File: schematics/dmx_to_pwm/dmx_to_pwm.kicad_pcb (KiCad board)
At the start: 2 copper layers, 11 parts, among them J4 PJ-031D, SW1 SW_SPST, SW2 SW_SPDT, U1 SN75176AP, U2 6N137, U3 6N137, U4 SN75176AP, U5 LM7812_TO220

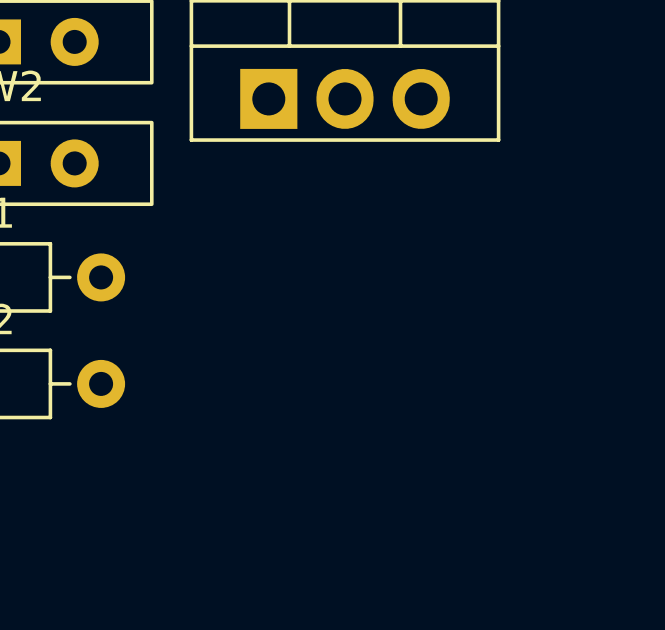
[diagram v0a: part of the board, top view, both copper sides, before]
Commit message: #5 improved schematics
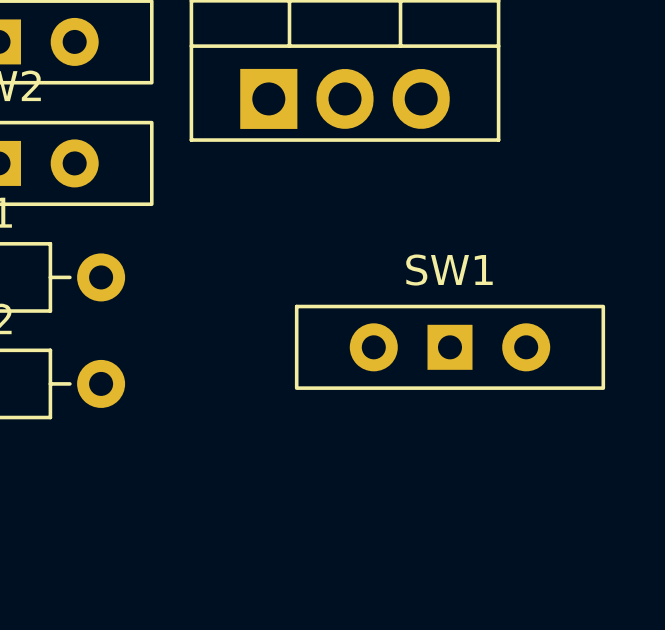
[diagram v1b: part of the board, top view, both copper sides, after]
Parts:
- added SW1: SW_SPDT, Button_Switch_THT:SW_Slide-03_Wuerth-WS-SLTV_10x2.5x6.4_P2.54mm, F.Cu at (109.2, 43.2)
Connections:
- D1 pad 2: Net-(D1-A) -> unconnected-(D1-A-Pad2)
- J4 pad 3: Net-(SW1-B) -> Net-(C3-Pad1)
- U5 pad 1: Net-(SW1-A) -> Net-(U5-VI)
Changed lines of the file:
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@@
 	(net 49 "Net-(U4-A)")
 	(net 50 "unconnected-(J4-Pad2)")
+	(net 51 "unconnected-(D1-A-Pad2)")
+	(net 52 "Net-(C3-Pad1)")
+	(net 53 "unconnected-(SW1-C-Pad2)")
+	(net 54 "Net-(U5-VI)")
 	(footprint "Button_Switch_THT:SW_Slide-03_Wuerth-WS-SLTV_10x2.5x6.4_P2.54mm"
 		(layer "F.Cu")
@@
 			(layers "*.Cu" "*.Mask")
 			(remove_unused_layers no)
-			(net 33 "Net-(SW1-B)")
+			(net 52 "Net-(C3-Pad1)")
 			(pinfunction "3")
 			(pintype "passive")
@@
 			(offset
 				(xyz -5.329999844 -0.09999999999 -2.579999885)
+			)
+			(scale
+				(xyz 1 1 1)
+			)
+			(rotate
+				(xyz 0 0 0)
+			)
+		)
+	)
+	(footprint "Button_Switch_THT:SW_Slide-03_Wuerth-WS-SLTV_10x2.5x6.4_P2.54mm"
+		(layer "F.Cu")
+		(at 109.22 43.18)
+		(descr "Wuerth, WS-SLTV, 450301014042, https://www.we-online.com/components/products/datasheet/450301014042.pdf")
+		(tags "switch single-pole double-throw SPDT würth wurth")
+		(property "Reference" "SW1"
+			(at 0 -2.54 0)
+			(layer "F.SilkS")
+			(effects
+				(font
+					(size 1 1)
+					(thickness 0.15)
+				)
+			)
+		)
+		(property "Value" "SW_SPDT"
+			(at 0 3.81 0)
+			(layer "F.Fab")
+			(effects
+				(font
+					(size 1 1)
+					(thickness 0.15)
+				)
+			)
+		)
+		(property "Footprint" "Button_Switch_THT:SW_Slide-03_Wuerth-WS-SLTV_10x2.5x6.4_P2.54mm"
+			(at 0 0 0)
+			(unlocked yes)
+			(layer "F.Fab")
+			(hide yes)
+			(effects
+				(font
+					(size 1.27 1.27)
+				)
+			)
+		)
+		(property "Datasheet" "https://www.we-online.com/components/products/datasheet/450301014042.pdf"
+			(at 0 0 0)
+			(unlocked yes)
+			(layer "F.Fab")
+			(hide yes)
+			(effects
+				(font
+					(size 1.27 1.27)
+				)
+			)
+		)
+		(property "Description" "Switch slide, single pole double throw"
+			(at 0 0 0)
+			(unlocked yes)
+			(layer "F.Fab")
+			(hide yes)
+			(effects
+				(font
+					(size 1.27 1.27)
+				)
+			)
+		)
+		(property ki_fp_filters "SW*Wuerth*WS*SLTV*10x2.5x6.4*P2.54mm*")
+		(sheetname "Root")
+		(sheetfile "dmx_to_pwm.kicad_sch")
+		(attr through_hole)
+		(fp_rect
+			(start -5.11 -1.36)
+			(end 5.11 1.36)
+			(stroke
+				(width 0.12)
+				(type default)
+			)
+			(fill none)
+			(layer "F.SilkS")
+		)
+		(fp_rect
+			(start -5.25 -1.5)
+			(end 5.25 1.5)
+			(stroke
+				(width 0.05)
+				(type default)
+			)
+			(fill none)
+			(layer "F.CrtYd")
+		)
+		(fp_rect
+			(start -5 -1.25)
+			(end 5 1.25)
+			(stroke
+				(width 0.1)
+				(type default)
+			)
+			(fill none)
+			(layer "F.Fab")
+		)
+		(fp_text user "${REFERENCE}"
+			(at 0 2.54 0)
+			(layer "F.Fab")
+			(effects
+				(font
+					(size 1 1)
+					(thickness 0.15)
+				)
+			)
+		)
+		(pad "1" thru_hole rect
+			(at 0 0)
+			(size 1.5 1.5)
+			(drill 0.8)
+			(layers "*.Cu" "*.Mask")
+			(remove_unused_layers no)
+			(net 33 "Net-(SW1-B)")
+			(pinfunction "B")
+			(pintype "passive")
+		)
+		(pad "2" thru_hole circle
+			(at -2.54 0)
+			(size 1.6 1.6)
+			(drill 0.8)
+			(layers "*.Cu" "*.Mask")
+			(remove_unused_layers no)
+			(net 53 "unconnected-(SW1-C-Pad2)")
+			(pinfunction "C")
+			(pintype "passive")
+		)
+		(pad "3" thru_hole circle
+			(at 2.54 0)
+			(size 1.6 1.6)
+			(drill 0.8)
+			(layers "*.Cu" "*.Mask")
+			(remove_unused_layers no)
+			(net 20 "VIN")
+			(pinfunction "A")
+			(pintype "passive")
+		)
+		(model "${KICAD8_3DMODEL_DIR}/Button_Switch_THT.3dshapes/SW_Slide-03_Wuerth-WS-SLTV_10x2.5x6.4_P2.54mm.wrl"
+			(offset
+				(xyz 0 0 0)
 			)
 			(scale
@@
 			(layers "*.Cu" "*.Mask")
 			(remove_unused_layers no)
-			(net 32 "Net-(SW1-A)")
+			(net 54 "Net-(U5-VI)")
 			(pinfunction "VI")
 			(pintype "power_in")
@@
 			(layers "*.Cu" "*.Mask")
 			(remove_unused_layers no)
-			(net 30 "Net-(D1-A)")
+			(net 51 "unconnected-(D1-A-Pad2)")
 			(pinfunction "A")
 			(pintype "passive")

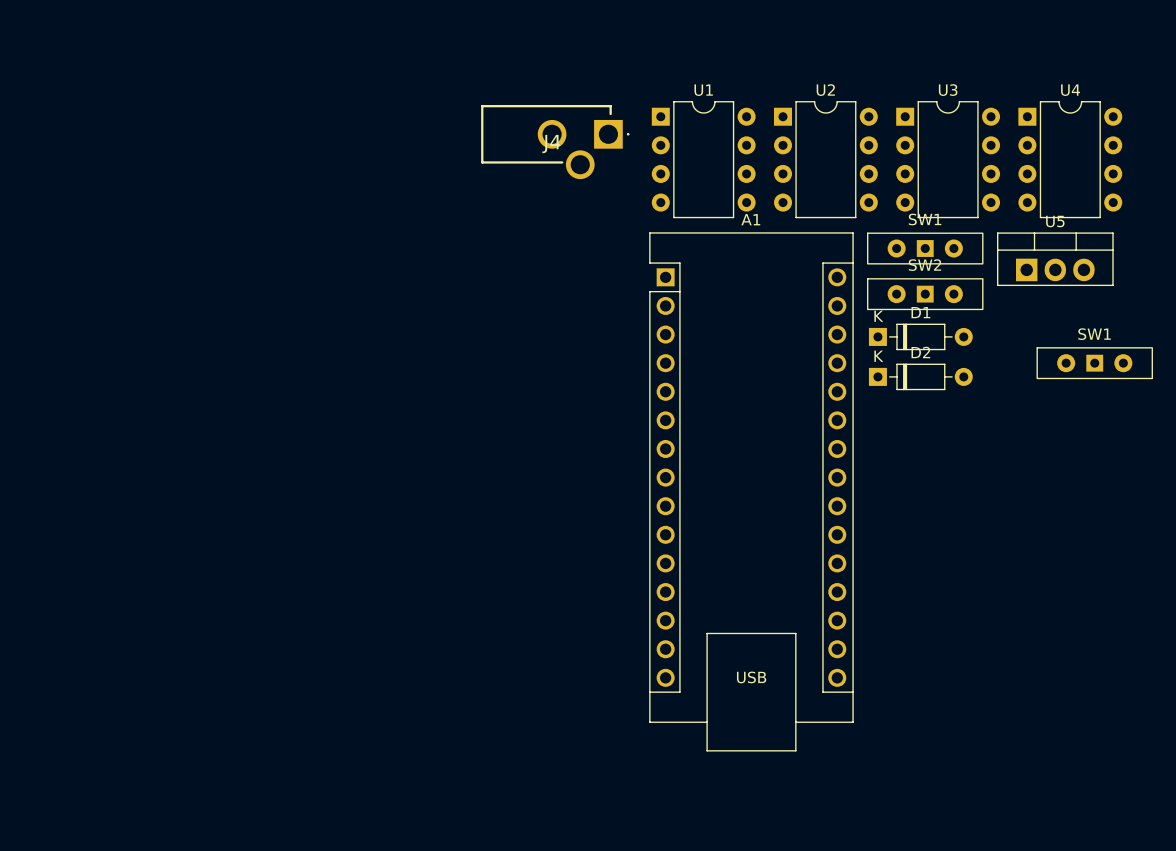
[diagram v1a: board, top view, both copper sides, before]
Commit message: updated schematics, added laser module blender file
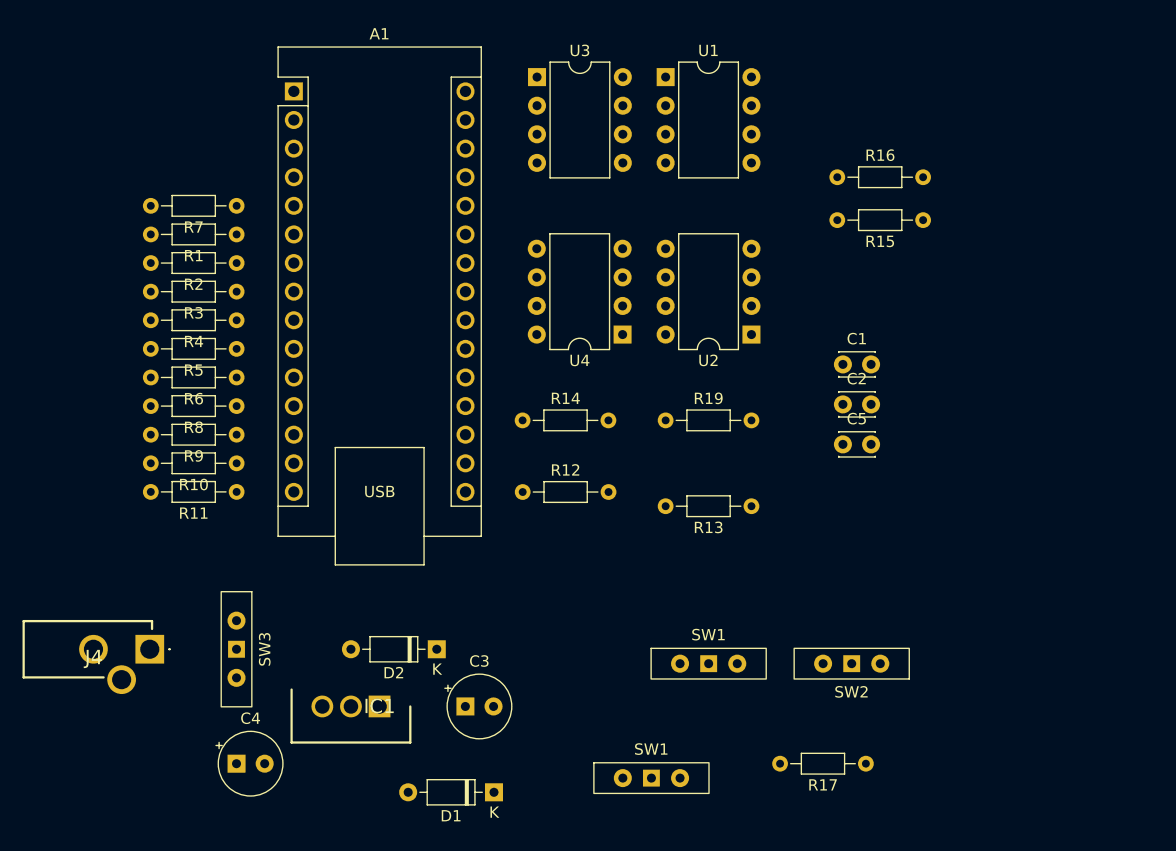
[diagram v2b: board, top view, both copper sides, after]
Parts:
- removed U5: LM7812_TO220, Package_TO_SOT_THT:TO-220-3_Vertical
- added C1: 100nF, Capacitor_THT:C_Disc_D3.0mm_W2.0mm_P2.50mm, F.Cu at (86.9, 43.3)
- added C2: 100nF, Capacitor_THT:C_Disc_D3.0mm_W2.0mm_P2.50mm, F.Cu at (86.9, 46.8)
- added C3: 10uF, Capacitor_THT:CP_Radial_Tantal_D5.5mm_P2.50mm, F.Cu at (53.3, 73.7)
- added C4: 330nF, Capacitor_THT:CP_Radial_Tantal_D5.5mm_P2.50mm, F.Cu at (33.0, 78.7)
- added C5: 100nF, Capacitor_THT:C_Disc_D3.0mm_W2.0mm_P2.50mm, F.Cu at (86.9, 50.4)
- added IC1: LM1085IT-12_NOPB, Lasers:TO254P470X1028X1955-3P, F.Cu at (45.7, 73.7)
- added R1: 1K, Resistor_THT:R_Axial_DIN0204_L3.6mm_D1.6mm_P7.62mm_Horizontal, F.Cu at (33.0, 31.8)
- added R10: 1K, Resistor_THT:R_Axial_DIN0204_L3.6mm_D1.6mm_P7.62mm_Horizontal, F.Cu at (33.0, 52.1)
- added R11: 1K, Resistor_THT:R_Axial_DIN0204_L3.6mm_D1.6mm_P7.62mm_Horizontal, F.Cu at (33.0, 54.6)
- added R12: 1K, Resistor_THT:R_Axial_DIN0204_L3.6mm_D1.6mm_P7.62mm_Horizontal, F.Cu at (58.4, 54.6)
- added R13: 470, Resistor_THT:R_Axial_DIN0204_L3.6mm_D1.6mm_P7.62mm_Horizontal, F.Cu at (78.7, 55.9)
- added R14: 4.7K, Resistor_THT:R_Axial_DIN0204_L3.6mm_D1.6mm_P7.62mm_Horizontal, F.Cu at (58.4, 48.3)
- added R15: 133, Resistor_THT:R_Axial_DIN0204_L3.6mm_D1.6mm_P7.62mm_Horizontal, F.Cu at (94.0, 30.5)
- added R16: 562, Resistor_THT:R_Axial_DIN0204_L3.6mm_D1.6mm_P7.62mm_Horizontal, F.Cu at (86.4, 26.7)
- added R17: 562, Resistor_THT:R_Axial_DIN0204_L3.6mm_D1.6mm_P7.62mm_Horizontal, F.Cu at (88.9, 78.7)
- added R19: 4.7K, Resistor_THT:R_Axial_DIN0204_L3.6mm_D1.6mm_P7.62mm_Horizontal, F.Cu at (71.1, 48.3)
- added R2: 1K, Resistor_THT:R_Axial_DIN0204_L3.6mm_D1.6mm_P7.62mm_Horizontal, F.Cu at (33.0, 34.3)
- added R3: 1K, Resistor_THT:R_Axial_DIN0204_L3.6mm_D1.6mm_P7.62mm_Horizontal, F.Cu at (33.0, 36.8)
- added R4: 1K, Resistor_THT:R_Axial_DIN0204_L3.6mm_D1.6mm_P7.62mm_Horizontal, F.Cu at (33.0, 39.4)
- added R5: 1K, Resistor_THT:R_Axial_DIN0204_L3.6mm_D1.6mm_P7.62mm_Horizontal, F.Cu at (33.0, 41.9)
- added R6: 1K, Resistor_THT:R_Axial_DIN0204_L3.6mm_D1.6mm_P7.62mm_Horizontal, F.Cu at (33.0, 44.5)
- added R7: 1K, Resistor_THT:R_Axial_DIN0204_L3.6mm_D1.6mm_P7.62mm_Horizontal, F.Cu at (33.0, 29.2)
- added R8: 1K, Resistor_THT:R_Axial_DIN0204_L3.6mm_D1.6mm_P7.62mm_Horizontal, F.Cu at (33.0, 47.0)
- added R9: 1K, Resistor_THT:R_Axial_DIN0204_L3.6mm_D1.6mm_P7.62mm_Horizontal, F.Cu at (33.0, 49.5)
- added SW3: SW_SPDT, Button_Switch_THT:SW_Slide-03_Wuerth-WS-SLTV_10x2.5x6.4_P2.54mm, F.Cu at (33.0, 68.6)
- moved J4 61.2 mm to (25.3, 68.6)
- moved SW1 52.9 mm to (69.9, 80.0)
- moved D1 52.9 mm to (55.9, 81.3), turned to 180 degrees
- moved D2 46.0 mm to (50.8, 68.6), turned to 180 degrees
- moved SW1 43.4 mm to (74.9, 69.9)
- moved U4 40.8 mm to (67.3, 40.6), turned to 180 degrees
- moved A1 36.9 mm to (38.1, 19.1)
- moved SW2 33.5 mm to (87.6, 69.9), turned to 180 degrees
- moved U3 32.9 mm to (59.7, 17.8)
- moved U2 19.5 mm to (78.7, 40.6), turned to 180 degrees
- moved U1 3.55 mm to (71.1, 17.8)
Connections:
- net Net-(U4-A) renamed DATA-_OUT
- net Net-(U4-B) renamed DATA+_OUT
- D1 pad 2: unconnected-(D1-A-Pad2) -> Net-(D1-A)
- J4 pad 3: Net-(C3-Pad1) -> TO_POE_UNREG
- U1 pad 6: Net-(U1-A) -> DATA+_IN
- U1 pad 7: Net-(U1-B) -> DATA-_IN
